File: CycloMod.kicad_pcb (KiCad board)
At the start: 4 copper layers, 22 x 22 mm, 47 parts, among them J1 MICROMOD-2222, U1 10CL010YM164, U2 W25Q128JVS, U3 1.2V, U4 RP2350_60QFN, U5 MIC5504-2.5YMT, Y1 ABM8-272-T3

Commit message: incremental edits
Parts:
- removed FD1, FD2, FD3, FD4: FIDUCIALUFIDUCIAL, MicroMod-RP2040-ProcessorBoard:FIDUCIAL-MICRO
- removed LOGO1: SFE_LOGO_NAME_FLAME.1_INCH, MicroMod-RP2040-ProcessorBoard:SFE_LOGO_NAME_FLAME_.1
- removed LOGO2: SFE_LOGO_FLAME.1_INCH, MicroMod-RP2040-ProcessorBoard:SFE_LOGO_FLAME_.1
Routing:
- net +2V5: track 2.67 -> 27.7 mm
- net Net-(U1E-VCCD_PLL1): track 4.68 -> 28.2 mm

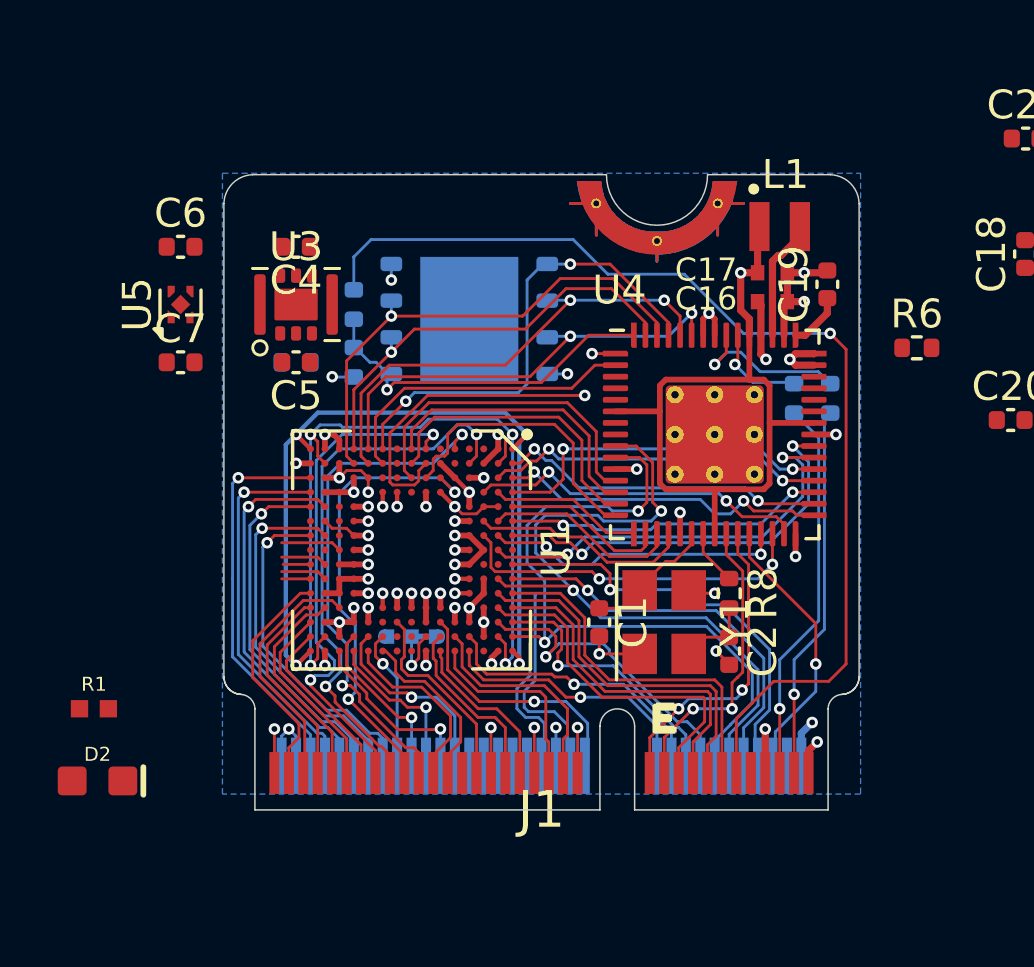
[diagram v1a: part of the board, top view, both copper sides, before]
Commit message: signals connected, still need to place decoupling
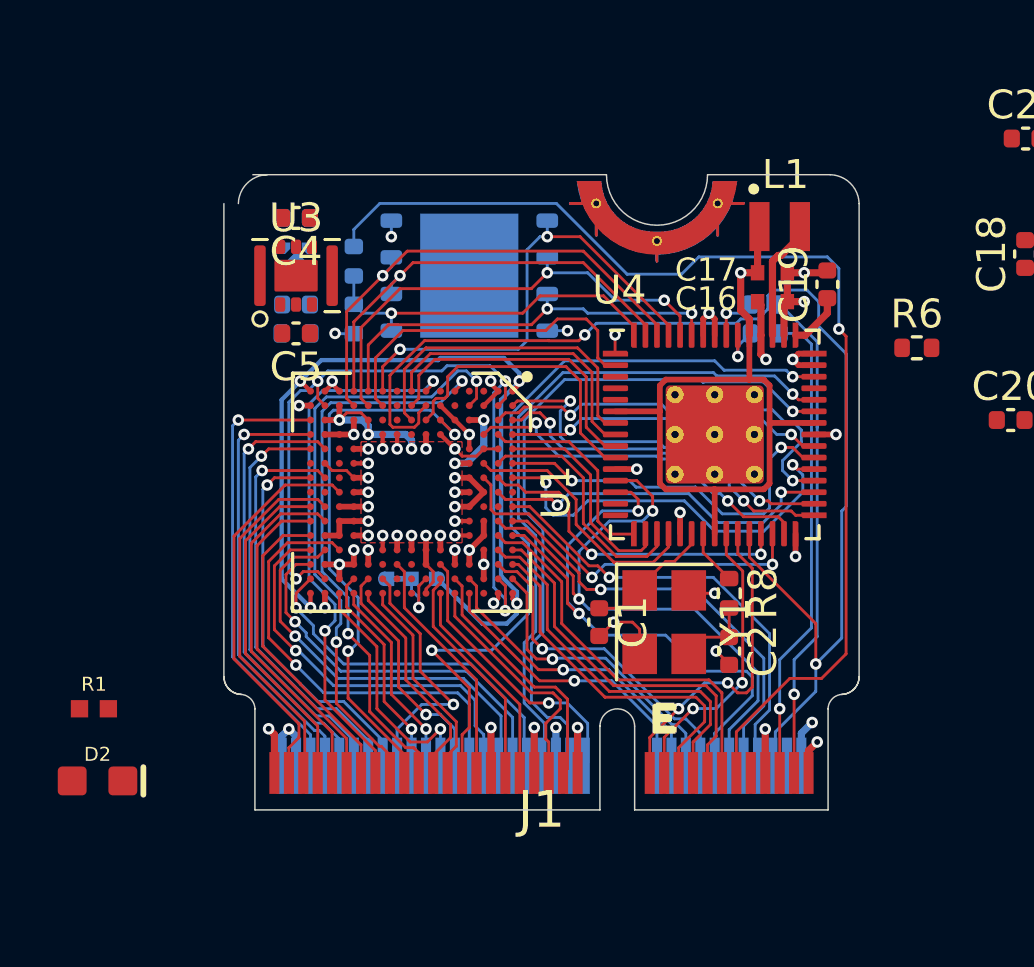
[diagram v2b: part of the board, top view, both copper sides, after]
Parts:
- C6, C7, U5: moved to B.Cu
- moved C7 4.47 mm to (140.0, 98.5), turned to 180 degrees
- moved U5 4.27 mm to (140.0, 97.0)
- moved C6 4.12 mm to (140.0, 95.5), turned to 180 degrees
- moved R12 3.95 mm to (156.2, 98.5), turned to 180 degrees
- moved R13 2.46 mm to (156.2, 99.5), turned to 180 degrees
- moved JP2 2.00 mm to (144.0, 108.0), turned to 0 degrees
- moved U1 2.00 mm to (144.0, 105.0)
- moved R5 1.50 mm to (142.0, 99.0)
- moved R7 1.50 mm to (142.0, 97.0)
- moved U2 1.50 mm to (146.0, 97.5)
- moved C4 1.00 mm to (140.0, 95.5)
- moved C5 1.00 mm to (140.0, 99.5)
- moved FB1 1.00 mm to (140.0, 99.5)
- moved U3 1.00 mm to (140.0, 97.5)
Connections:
- U1 pad A11: /RTS1 -> /SCL
- U1 pad A12: /TX1 -> /CTS1
- U1 pad A13: /D1 -> /RX1
- U1 pad A14: /SCL -> /D1
- U1 pad A4: /CLKOUT1 -> /CLKOUT3
- U1 pad A6: /CLKOUT0 -> /CLKOUT2
- U1 pad A7: /CLKOUT3 -> /CLKOUT1
- U1 pad B11: /CTS1 -> /RTS1
- U1 pad B12: /RX1 -> /TX1
- U1 pad B8: /CLKOUT2 -> /CLKOUT0
- U1 pad N12: /G6 -> /G4
- U1 pad N8: /G1 -> /G5
- U1 pad P10: /G3 -> /G8
- U1 pad P12: /G8 -> /G2
- U1 pad P9: /G2 -> /G6
- U1 pad R10: /G4 -> /G9
- U1 pad R11: /G5 -> /G10
- U1 pad R12: /G7 -> /G3
- U1 pad R13: /G9 -> /G1
- U1 pad R14: /G10 -> /G0
- U1 pad R9: /G0 -> /G7
- U4 pad 10: /SCL -> /TDI
- U4 pad 12: /TDO -> /SDA
- U4 pad 13: /TMS -> /SCL
- U4 pad 14: /TCK -> /GPIO10
- U4 pad 15: /TDI -> /GPIO11
- U4 pad 7: /GPIO4 -> /TDO
- U4 pad 8: /GPIO5 -> /TMS
- U4 pad 9: /SDA -> /TCK
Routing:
- net /BATT_VIN/3: track 0.00 -> 27.4 mm, vias 0 -> 2
- net /~{RESET}: track 20.4 -> 43.0 mm
- net /A1: track 5.12 -> 24.1 mm, vias 0 -> 1
- net /A0: track 7.28 -> 24.3 mm, vias 0 -> 1
- net /G4: track 1.00 -> 15.5 mm, vias 0 -> 1
- net /G2: track 1.60 -> 14.4 mm, vias 0 -> 1
- net /G3: track 1.60 -> 14.0 mm, vias 0 -> 1
- net /G0: track 0.95 -> 12.6 mm, vias 0 -> 1
- net /G1: track 2.10 -> 13.4 mm, vias 0 -> 1
- net /G5: track 8.07 -> 13.8 mm
- net +1V2: track 7.21 -> 12.6 mm, vias 11 -> 12
- net /G9: track 6.61 -> 11.4 mm
- net /G10: track 6.14 -> 10.9 mm
- net /G8: track 7.51 -> 12.2 mm
- net /G7: track 7.19 -> 11.8 mm
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- added copper zone on F.Cu, net +1V2
- removed copper zone on B.Cu, net GND
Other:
- outline, holes or cut-outs redrawn

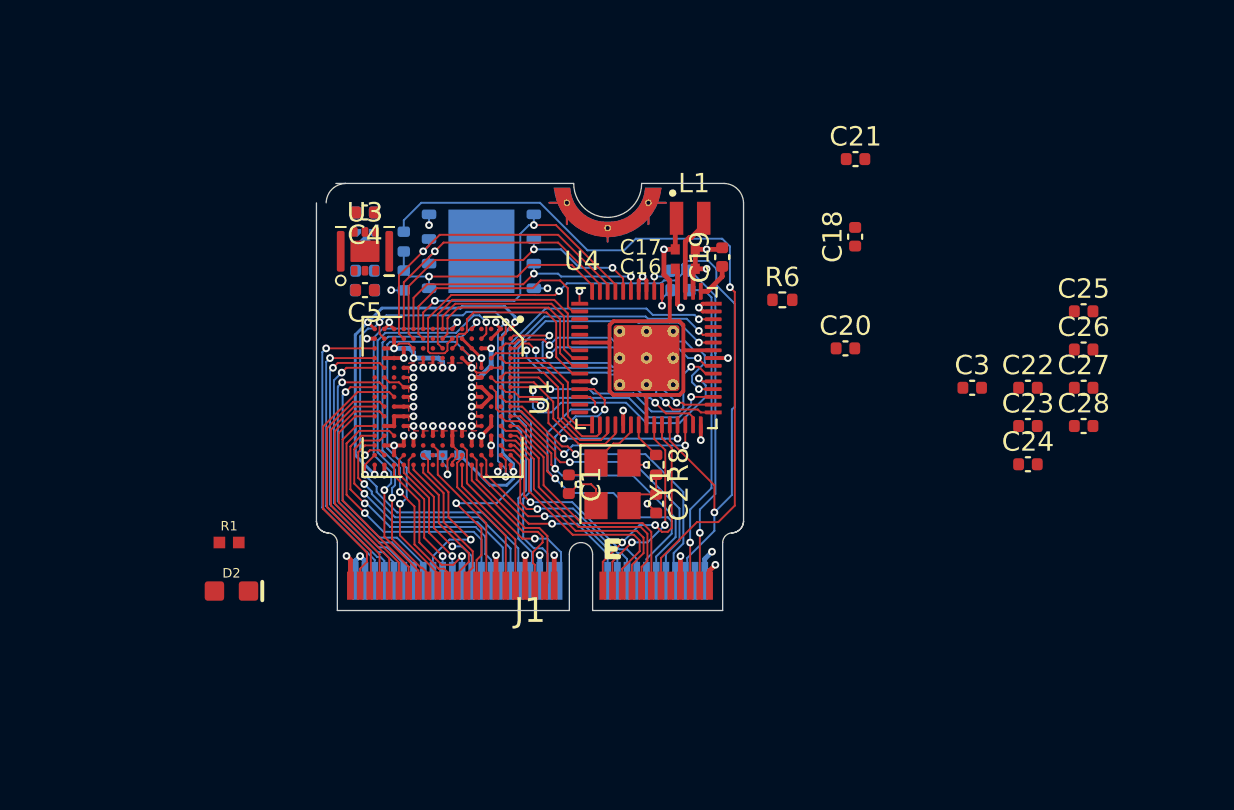
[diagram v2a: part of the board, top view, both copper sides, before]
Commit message: more routing and added decoupling caps for FPGA
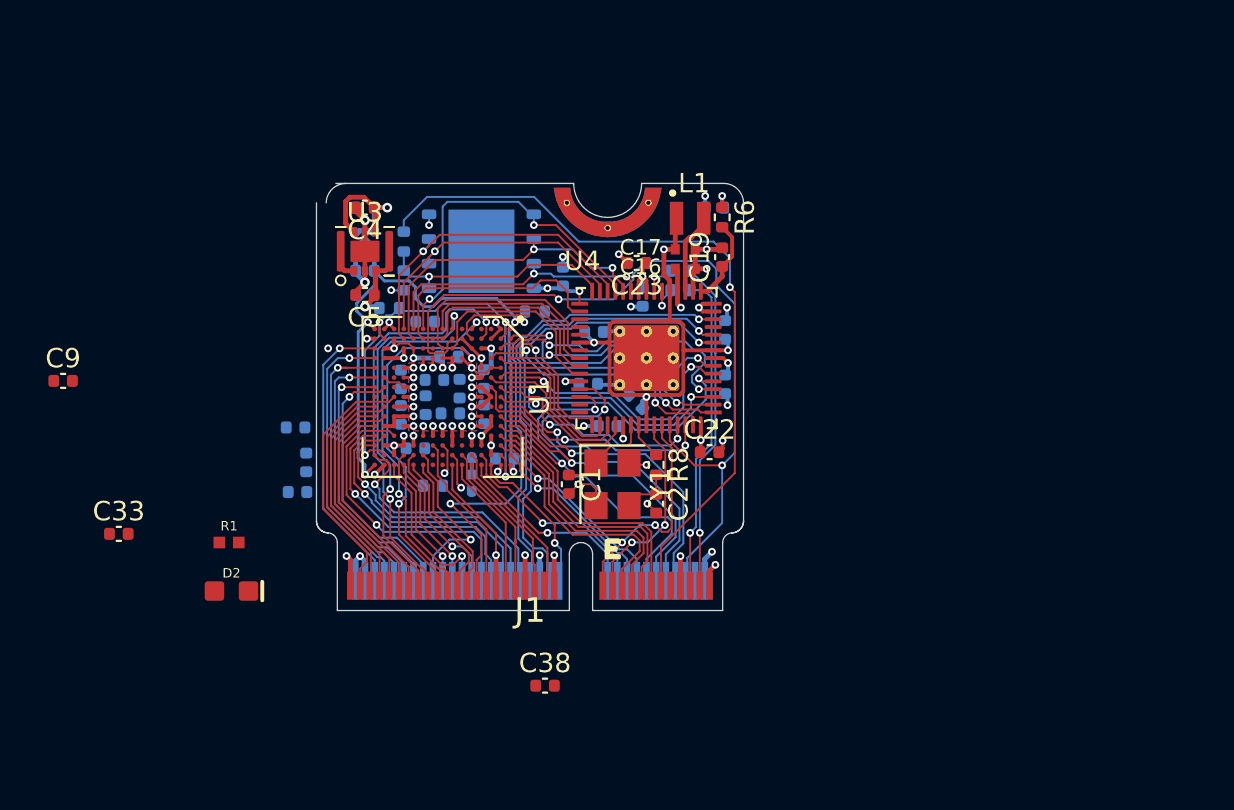
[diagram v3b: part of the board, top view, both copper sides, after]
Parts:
- added C10: 100n, Capacitor_SMD:C_0402_1005Metric, B.Cu at (146.2, 105.9)
- added C11: 100n, Capacitor_SMD:C_0402_1005Metric, B.Cu at (144.9, 104.6)
- added C12: 100n, Capacitor_SMD:C_0402_1005Metric, B.Cu at (141.8, 105.9)
- added C13: 100n, Capacitor_SMD:C_0402_1005Metric, B.Cu at (143.6, 104.1)
- added C14: 100n, Capacitor_SMD:C_0402_1005Metric, B.Cu at (147.2, 108.2)
- added C15: 100n, Capacitor_SMD:C_0402_1005Metric, B.Cu at (136.5, 109.9)
- added C29: 1u, Capacitor_SMD:C_0402_1005Metric, B.Cu at (143.1, 101.1)
- added C30: 100n, Capacitor_SMD:C_0402_1005Metric, B.Cu at (137.0, 108.4)
- added C31: 100n, Capacitor_SMD:C_0402_1005Metric, B.Cu at (136.4, 106.6)
- added C32: 4.7u, Capacitor_SMD:C_0402_1005Metric, B.Cu at (144.3, 102.9)
- added C33: 1u, Capacitor_SMD:C_0402_1005Metric, F.Cu at (127.3, 112.1)
- added C34: 100n, Capacitor_SMD:C_0402_1005Metric, B.Cu at (144.4, 105.8)
- added C35: 100n, Capacitor_SMD:C_0402_1005Metric, B.Cu at (143.1, 105.4)
- added C36: 100n, Capacitor_SMD:C_0402_1005Metric, B.Cu at (146.1, 104.1)
- added C37: 100n, Capacitor_SMD:C_0402_1005Metric, B.Cu at (141.8, 104.1)
- added C38: 4.7u, Capacitor_SMD:C_0402_1005Metric, F.Cu at (149.3, 119.9)
- added C8: 4.7u, Capacitor_SMD:C_0402_1005Metric, B.Cu at (142.6, 107.7)
- added C9: 1u, Capacitor_SMD:C_0402_1005Metric, F.Cu at (124.5, 104.2)
- added R2: 10k, Resistor_SMD:R_0402_1005Metric, B.Cu at (143.5, 109.6)
- added R3: 10k, Resistor_SMD:R_0402_1005Metric, B.Cu at (148.8, 100.6)
- C18, C20, C21, C24, C25, C26, C27, C28, C3: moved to B.Cu
- moved C25 26.9 mm to (150.2, 98.8), turned to 90 degrees
- moved C26 25.6 mm to (151.5, 104.3)
- moved C28 23.7 mm to (154.3, 99.8), turned to -90 degrees
- moved C23 21.8 mm to (154.0, 98.1), turned to 180 degrees
- moved C24 21.7 mm to (152.5, 106.5), turned to 180 degrees
- moved C27 21.2 mm to (158.0, 95.2), turned to 180 degrees
- moved C21 16.9 mm to (153.9, 105.2), turned to 135 degrees
- moved C22 16.7 mm to (157.8, 107.8)
- moved C20 13.0 mm to (151.8, 101.7)
- moved C3 12.7 mm to (158.6, 104.3), turned to -90 degrees
- moved C18 8.24 mm to (158.6, 101.5)
- moved R6 5.26 mm to (158.4, 95.8), turned to -90 degrees
- moved JP2 1.80 mm to (145.5, 109.0), turned to -90 degrees
- moved FB1 1.56 mm to (141.2, 100.4), turned to 0 degrees
- moved C4 0.25 mm to (140.0, 95.2)
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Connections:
- U1 pad C15: unconnected-(U1C-IO_C15_DR2N-PadC15) -> /PWM0
- U1 pad E2: unconnected-(U1A-NSTATUS-PadE2) -> /nSTATUS
- U1 pad F13: /PWM0 -> unconnected-(U1C-IO_F13_DR17N_INITDONE-PadF13)
- U1 pad F14: /CAN_TX -> /CAN_RX
- U1 pad F15: /CAN_RX -> /CAN_TX
- U1 pad H13: unconnected-(U1C-CONF_DONE-PadH13) -> /DONE
- U1 pad H4: unconnected-(U1A-NCE-PadH4) -> GND
- U1 pad P10: /G8 -> /G9
- U1 pad P5: /SDIO_DAT1 -> unconnected-(U1B-IO_P5_PLL1CLKOUTP-PadP5)
- U1 pad P7: /SPI_COPI1/SDIO_CMD -> /SPI_SCK1/SDIO_CLK
- U1 pad P9: /G6 -> /G7
- U1 pad R10: /G9 -> /G8
- U1 pad R5: /SPI_CIPO1/SDIO_DAT0 -> /SDIO_DAT1
- U1 pad R6: unconnected-(U1B-IO_R6-PadR6) -> /SPI_CIPO1/SDIO_DAT0
- U1 pad R7: /SPI_SCK1/SDIO_CLK -> /SPI_COPI1/SDIO_CMD
- U1 pad R9: /G7 -> /G6
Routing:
- net GND: track 39.8 -> 60.4 mm, vias 33 -> 44
- net +3V3: track 22.0 -> 37.4 mm, vias 19 -> 21
- net +1V2: track 12.6 -> 23.4 mm, vias 12 -> 13
- net /nSTATUS: track 0.00 -> 5.36 mm, vias 0 -> 1
- net +1V1: track 25.4 -> 28.2 mm, vias 1 -> 4
- net /VREG_AVDD: track 1.94 -> 4.38 mm
- net /PWM0: track 9.89 -> 7.89 mm
- net /QSPI_SD0: track 16.6 -> 18.3 mm
- net /DONE: track 0.00 -> 1.59 mm, vias 0 -> 1
- net Net-(U3-L1): track 0.00 -> 1.58 mm
- net /~{BOOT}: track 39.0 -> 37.7 mm
- net /~{RESET}: track 43.0 -> 41.9 mm
- net /SDA: track 22.0 -> 23.0 mm
- net /G8: track 12.2 -> 11.2 mm
- net /CLKIN0: track 13.6 -> 14.6 mm
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
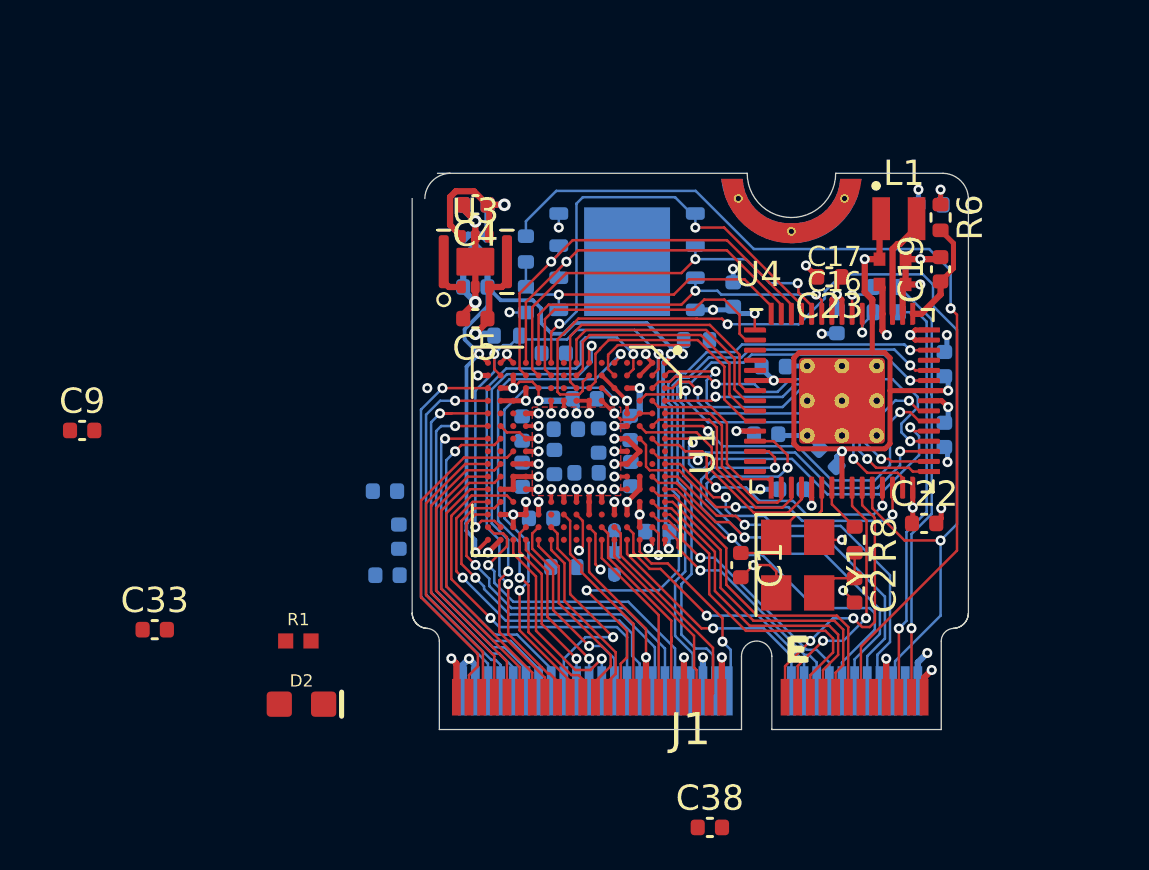
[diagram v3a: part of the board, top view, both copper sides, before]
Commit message: more cleanup, decoupling caps in, a couple nets need connecting, more cleanup to go
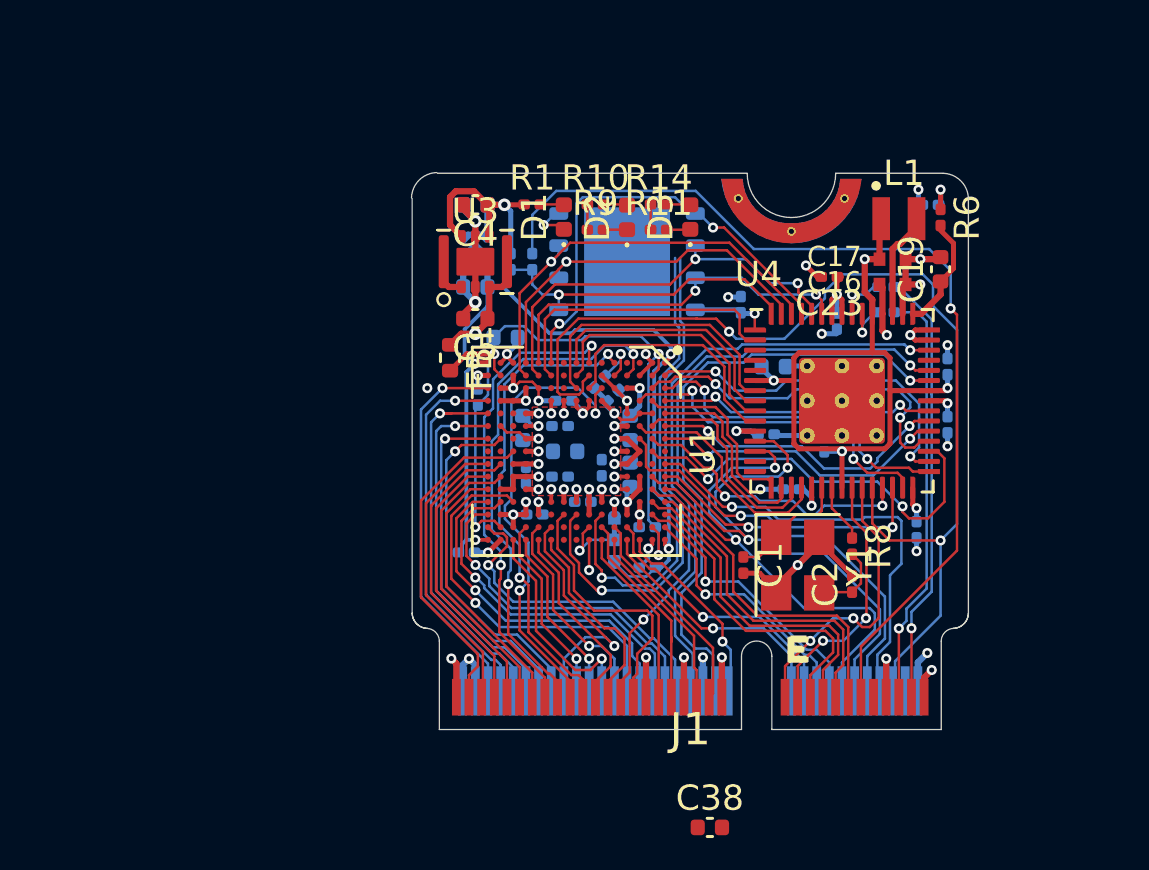
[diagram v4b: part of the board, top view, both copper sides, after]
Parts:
- removed R2: 10k, Resistor_SMD:R_0402_1005Metric
- added D1: LED, LED_SMD:LED_0402_1005Metric, F.Cu at (143.5, 95.7)
- added D3: LED, LED_SMD:LED_0402_1005Metric, F.Cu at (148.5, 95.7)
- added R10: 1k, Resistor_SMD:R_0201_0603Metric, F.Cu at (144.8, 95.2)
- added R11: 10k, Resistor_SMD:R_0201_0603Metric, F.Cu at (147.2, 96.2)
- added R14: 1k, Resistor_SMD:R_0201_0603Metric, F.Cu at (147.2, 95.2)
- added R9: 10k, Resistor_SMD:R_0201_0603Metric, F.Cu at (144.8, 96.2)
- C1, C10, C11, C12, C13, C14, C15, C18, C2, C21, C23, C24, C25, C26, C27, C28, C3, C30, C31, C34, C35, C36, C37: footprint Capacitor_SMD:C_0402_1005Metric -> Capacitor_SMD:C_0201_0603Metric
- C22: footprint Capacitor_SMD:C_0402_1005Metric -> Capacitor_SMD:C_0201_0603Metric; moved to B.Cu
- C33, C9: moved to B.Cu
- D2: value BLUE -> LED; footprint MicroMod-RP2040-ProcessorBoard:LED-0603 -> LED_SMD:LED_0402_1005Metric
- FB1: moved to F.Cu
- R1: value 1KOHM-0402T-1/16W-1% -> 1k; footprint MicroMod-RP2040-ProcessorBoard:0402-TIGHT -> Resistor_SMD:R_0201_0603Metric
- R12, R13, R3, R5, R6, R7, R8: footprint Resistor_SMD:R_0402_1005Metric -> Resistor_SMD:R_0201_0603Metric
- moved D2 23.2 mm to (146.0, 95.8), turned to 90 degrees
- moved C33 20.4 mm to (146.1, 104.1), turned to -90 degrees
- moved R1 19.6 mm to (142.2, 95.2)
- moved C9 17.4 mm to (141.9, 104.1), turned to -90 degrees
- moved C30 9.83 mm to (146.8, 108.0), turned to 180 degrees
- moved C31 5.23 mm to (140.1, 102.8), turned to 90 degrees
- moved R3 4.19 mm to (144.9, 102.2), turned to 45 degrees
- moved C10 4.12 mm to (142.3, 107.5), turned to 180 degrees
- moved C8 3.92 mm to (146.1, 105.9), turned to 90 degrees
- moved C37 3.76 mm to (144.2, 107.0), turned to 0 degrees
- moved C15 3.25 mm to (139.7, 109.0)
- moved C36 2.84 mm to (143.5, 103.0), turned to 0 degrees
- moved FB1 2.41 mm to (139.0, 101.3), turned to -90 degrees
- moved C32 2.22 mm to (143.6, 105.0)
- moved C29 2.00 mm to (141.2, 100.5), turned to 0 degrees
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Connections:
- R1 pad 1: Net-(D2-PadA) -> +3V3
- R1 pad 2: /LED_BUILTIN/G10 -> Net-(D1-A)
- U1 pad F13: unconnected-(U1C-IO_F13_DR17N_INITDONE-PadF13) -> /INIT
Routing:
- net /INIT: track 0.00 -> 19.8 mm, vias 0 -> 1
- net /DONE: track 1.59 -> 21.0 mm
- net +3V3: track 37.4 -> 45.3 mm, vias 21 -> 19
- net GND: track 60.4 -> 67.5 mm, vias 44 -> 43
- net /CLKOUT0: track 12.7 -> 16.2 mm
- net /nSTATUS: track 5.36 -> 2.09 mm
- net Net-(U1E-VCCD_PLL1): track 26.9 -> 29.8 mm
- net /BATT_VIN/3: track 27.6 -> 24.7 mm
- net +2V5: track 31.7 -> 34.5 mm
- net /CLKOUT1: track 14.7 -> 11.9 mm
- net /PWM1: track 8.36 -> 10.4 mm
- net /G11: track 15.8 -> 17.5 mm
- net /CLKOUT2: track 13.6 -> 12.0 mm
- net /SPI_MOSI: track 21.8 -> 20.8 mm
- net +1V2: track 23.4 -> 22.4 mm, vias 13 -> 12
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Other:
- outline, holes or cut-outs redrawn
